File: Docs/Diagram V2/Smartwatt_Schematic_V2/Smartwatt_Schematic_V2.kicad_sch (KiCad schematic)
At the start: 21 parts, among them J1 Power Input, J10 Power Input, J11 Power Input, J12 Power Input, J13 Water Level, J2 Screw_Terminal_01x03, J3 Power Input, J4 Power Input, J5 Water Level, J6 Water Level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

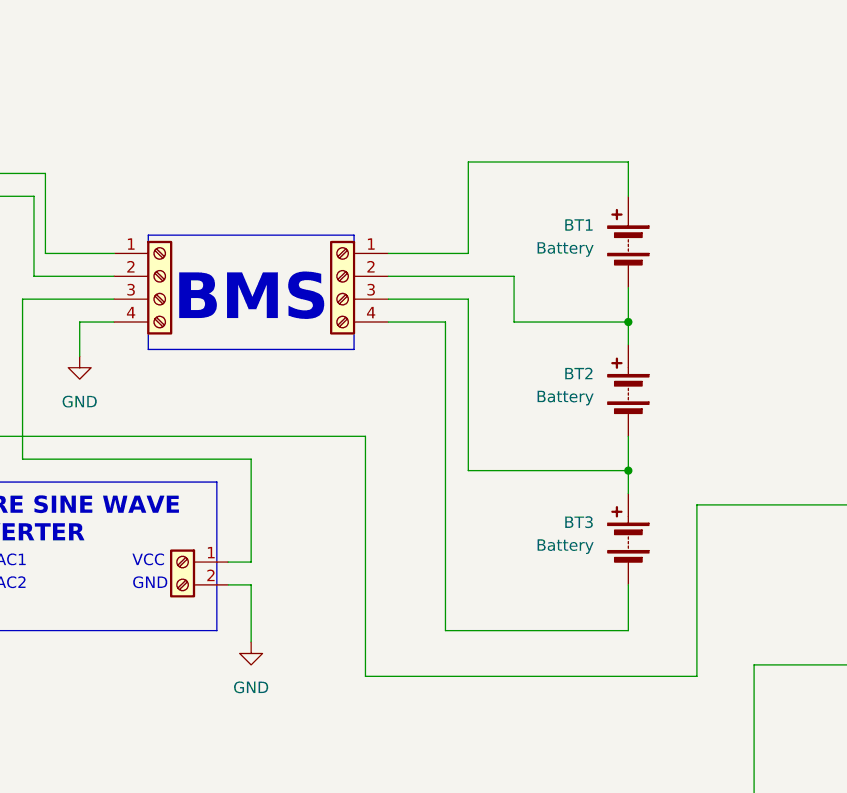
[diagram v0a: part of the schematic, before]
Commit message: Enhances kWh data precision and updates schematic
Improves the accuracy of energy consumption values displayed throughout the web application and in monthly report exports. All kWh readings, including dashboard metrics, monthly summaries, daily breakdowns, and CSV/PDF reports, now show three decimal places. This provides users with more granular energy usage information.

Updates the Smartwatt V2 schematic to reflect changes in the power management section. Renames the 'BMS' component to 'Charge Controller', adds a 'BATTERY' label for clarity, refines battery connection points, and removes redundant components to streamline the diagram.
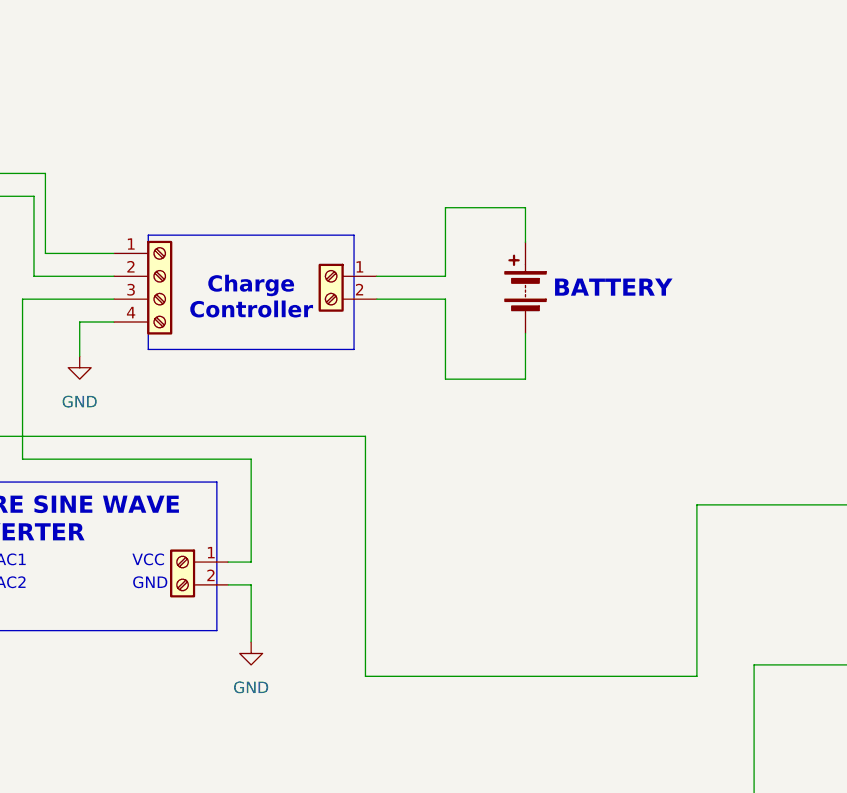
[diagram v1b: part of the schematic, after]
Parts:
- removed BT2, BT3: Battery, symbol Device:Battery
- removed J5: Water Level, symbol Connector:Screw_Terminal_01x04
- added J14: Power Input, symbol Connector:Screw_Terminal_01x02
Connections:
- net at BT1.1 (+): now also J14.1 (Pin_1)
- net at BT1.2 (-): now also J14.2 (Pin_2)
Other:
- note added: "BATTERY"
- note added: "Charge Controller"
- note removed: "BMS"
